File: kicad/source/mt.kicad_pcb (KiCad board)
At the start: 4 copper layers, 166.4 x 142.2 mm, 138 parts, among them IC1 MCP73831T-2ACI_OT, IC10 SN74HC148NSR, IC11 SN74HC148NSR, IC2 BQ29728DSER, IC3 TLV74333PDBVR, IC4 TLV9152IDR, IC5 MSPM0G3507SPMR, IC6 IS62WV1288BLL-55QLI, IC7 DAC082S085CIMMX_NOPB, IC8 SN74HC148NSR, IC9 SN74HC148NSR, J1 694106301002, J10 Conn_01x02_Pin, J2 3557-2, J3 SJ1-3524N, J4 Conn_01x05_Pin, J5 Conn_01x09_Pin, J6 Conn_01x03_Pin, J7 Conn_01x03_Pin, J8 Conn_01x03_Pin, J9 Conn_01x02_Pin, Q1 CSD16406Q3, Q2 CSD16406Q3, U1 1043

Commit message: misc adjustments
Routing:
- net GND: track 38.4 -> 42.3 mm, vias 14 -> 16
- net E2_2: track 83.4 -> 84.4 mm
- net Net-(IC11-6): track 59.2 -> 59.9 mm
- net E1_0: track 68.3 -> 67.8 mm

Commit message: completed PCB fab setup
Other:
- board text added: "5.5mm x 2.1mm 5V Only"
- board text removed: "6.5mm x 2.1mm 5V Only"
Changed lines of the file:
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@@
 			(outputformat 1)
 			(mirror no)
-			(drillshape 1)
+			(drillshape 0)
 			(scaleselection 1)
-			(outputdirectory "")
+			(outputdirectory "mt-fab/")
 		)
 	)
@@
 		(sheetname "/Rank 0/")
 		(sheetfile "rank.kicad_sch")
-		(attr smd)
+		(attr smd dnp)
 		(fp_line
 			(start -5.3 -2)
@@
 		(sheetname "/Rank 0/")
 		(sheetfile "rank.kicad_sch")
-		(attr smd)
+		(attr smd dnp)
 		(fp_line
 			(start -5.3 -2)
@@
 		(sheetname "/Rank 2/")
 		(sheetfile "rank.kicad_sch")
-		(attr smd)
+		(attr smd dnp)
 		(fp_line
 			(start -5.3 -2)
@@
 		(sheetname "/Rank 1/")
 		(sheetfile "rank.kicad_sch")
-		(attr smd)
+		(attr smd dnp)
 		(fp_line
 			(start -5.3 -2)
@@
 		(sheetname "/Rank 3/")
 		(sheetfile "rank.kicad_sch")
-		(attr smd)
+		(attr smd dnp)
 		(fp_line
 			(start -5.3 -2)
@@
 		(sheetname "/Rank 0/")
 		(sheetfile "rank.kicad_sch")
-		(attr smd)
+		(attr smd dnp)
 		(fp_line
 			(start -5.3 -2)
@@
 		(sheetname "/Rank 2/")
 		(sheetfile "rank.kicad_sch")
-		(attr smd)
+		(attr smd dnp)
 		(fp_line
 			(start -5.3 -2)
@@
 		(sheetname "/")
 		(sheetfile "mt.kicad_sch")
-		(attr smd)
+		(attr smd dnp)
 		(fp_line
 			(start -5.3 -2)
@@
 		(sheetname "/Rank 3/")
 		(sheetfile "rank.kicad_sch")
-		(attr smd)
+		(attr smd dnp)
 		(fp_line
 			(start -5.3 -2)
@@
 		(sheetname "/Rank 2/")
 		(sheetfile "rank.kicad_sch")
-		(attr smd)
+		(attr smd dnp)
 		(fp_line
 			(start -5.3 -2)
@@
 		(sheetname "/Rank 2/")
 		(sheetfile "rank.kicad_sch")
-		(attr smd)
+		(attr smd dnp)
 		(fp_line
 			(start -5.3 -2)
@@
 		(sheetname "/Rank 1/")
 		(sheetfile "rank.kicad_sch")
-		(attr smd)
+		(attr smd dnp)
 		(fp_line
 			(start -5.3 -2)
@@
 		(sheetname "/Rank 3/")
 		(sheetfile "rank.kicad_sch")
-		(attr smd)
+		(attr smd dnp)
 		(fp_line
 			(start -5.3 -2)
@@
 		(sheetname "/Rank 2/")
 		(sheetfile "rank.kicad_sch")
-		(attr smd)
+		(attr smd dnp)
 		(fp_line
 			(start -5.3 -2)
@@
 		(sheetname "/Rank 0/")
 		(sheetfile "rank.kicad_sch")
-		(attr smd)
+		(attr smd dnp)
 		(fp_line
 			(start -5.3 -2)
@@
 		(sheetname "/Rank 2/")
 		(sheetfile "rank.kicad_sch")
-		(attr smd)
+		(attr smd dnp)
 		(fp_line
 			(start -5.3 -2)
@@
 		(sheetname "/Rank 1/")
 		(sheetfile "rank.kicad_sch")
-		(attr smd)
+		(attr smd dnp)
 		(fp_line
 			(start -5.3 -2)
@@
 		(sheetname "/Rank 1/")
 		(sheetfile "rank.kicad_sch")
-		(attr smd)
+		(attr smd dnp)
 		(fp_line
 			(start -5.3 -2)
@@
 		(sheetname "/Rank 0/")
 		(sheetfile "rank.kicad_sch")
-		(attr smd)
+		(attr smd dnp)
 		(fp_line
 			(start -5.3 -2)
@@
 		(sheetname "/Rank 3/")
 		(sheetfile "rank.kicad_sch")
-		(attr smd)
+		(attr smd dnp)
 		(fp_line
 			(start -5.3 -2)
@@
 		(sheetname "/Rank 3/")
 		(sheetfile "rank.kicad_sch")
-		(attr smd)
+		(attr smd dnp)
 		(fp_line
 			(start -5.3 -2)
@@
 		(sheetname "/Rank 1/")
 		(sheetfile "rank.kicad_sch")
-		(attr smd)
+		(attr smd dnp)
 		(fp_line
 			(start -5.3 -2)
@@
 		(sheetname "/Rank 2/")
 		(sheetfile "rank.kicad_sch")
-		(attr smd)
+		(attr smd dnp)
 		(fp_line
 			(start -5.3 -2)
@@
 		(sheetname "/Rank 1/")
 		(sheetfile "rank.kicad_sch")
-		(attr smd)
+		(attr smd dnp)
 		(fp_line
 			(start -5.3 -2)
@@
 		(sheetname "/Rank 0/")
 		(sheetfile "rank.kicad_sch")
-		(attr smd)
+		(attr smd dnp)
 		(fp_line
 			(start -5.3 -2)
@@
 		(sheetname "/Rank 3/")
 		(sheetfile "rank.kicad_sch")
-		(attr smd)
+		(attr smd dnp)
 		(fp_line
 			(start -5.3 -2)
@@
 		(sheetname "/Rank 1/")
 		(sheetfile "rank.kicad_sch")
-		(attr smd)
+		(attr smd dnp)
 		(fp_line
 			(start -5.3 -2)
@@
 		(sheetname "/Rank 3/")
 		(sheetfile "rank.kicad_sch")
-		(attr smd)
+		(attr smd dnp)
 		(fp_line
 			(start -5.3 -2)
@@
 		(sheetname "/")
 		(sheetfile "mt.kicad_sch")
-		(attr smd)
+		(attr smd dnp)
 		(fp_line
 			(start -5.3 -2)
@@
 		(sheetname "/Rank 0/")
 		(sheetfile "rank.kicad_sch")
-		(attr smd)
+		(attr smd dnp)
 		(fp_line
 			(start -5.3 -2)
@@
 		(sheetname "/Rank 2/")
 		(sheetfile "rank.kicad_sch")
-		(attr smd)
+		(attr smd dnp)
 		(fp_line
 			(start -5.3 -2)
@@
 		(sheetname "/Rank 3/")
 		(sheetfile "rank.kicad_sch")
-		(attr smd)
+		(attr smd dnp)
 		(fp_line
 			(start -5.3 -2)
@@
 		(sheetname "/Rank 0/")
 		(sheetfile "rank.kicad_sch")
-		(attr smd)
+		(attr smd dnp)
 		(fp_line
 			(start -5.3 -2)
@@
 		(sheetname "/Rank 1/")
 		(sheetfile "rank.kicad_sch")
-		(attr smd)
+		(attr smd dnp)
 		(fp_line
 			(start -5.3 -2)
@@
 		)
 	)
-	(gr_text "6.5mm x\n2.1mm\n5V Only"
+	(gr_text "5.5mm x\n2.1mm\n5V Only"
 		(at 56.515 38.735 0)
 		(layer "F.SilkS")

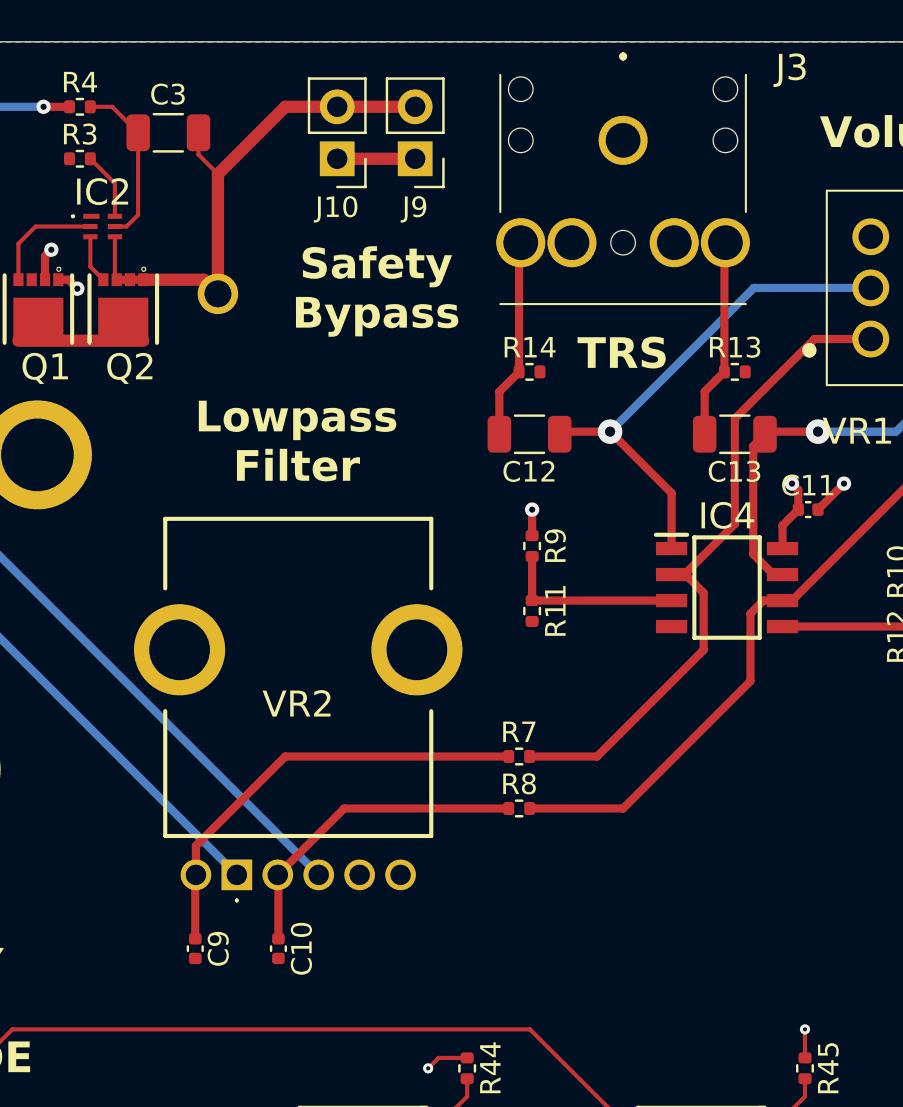
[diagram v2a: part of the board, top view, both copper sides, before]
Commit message: adjusted PCB fab setup for faster manufacturing
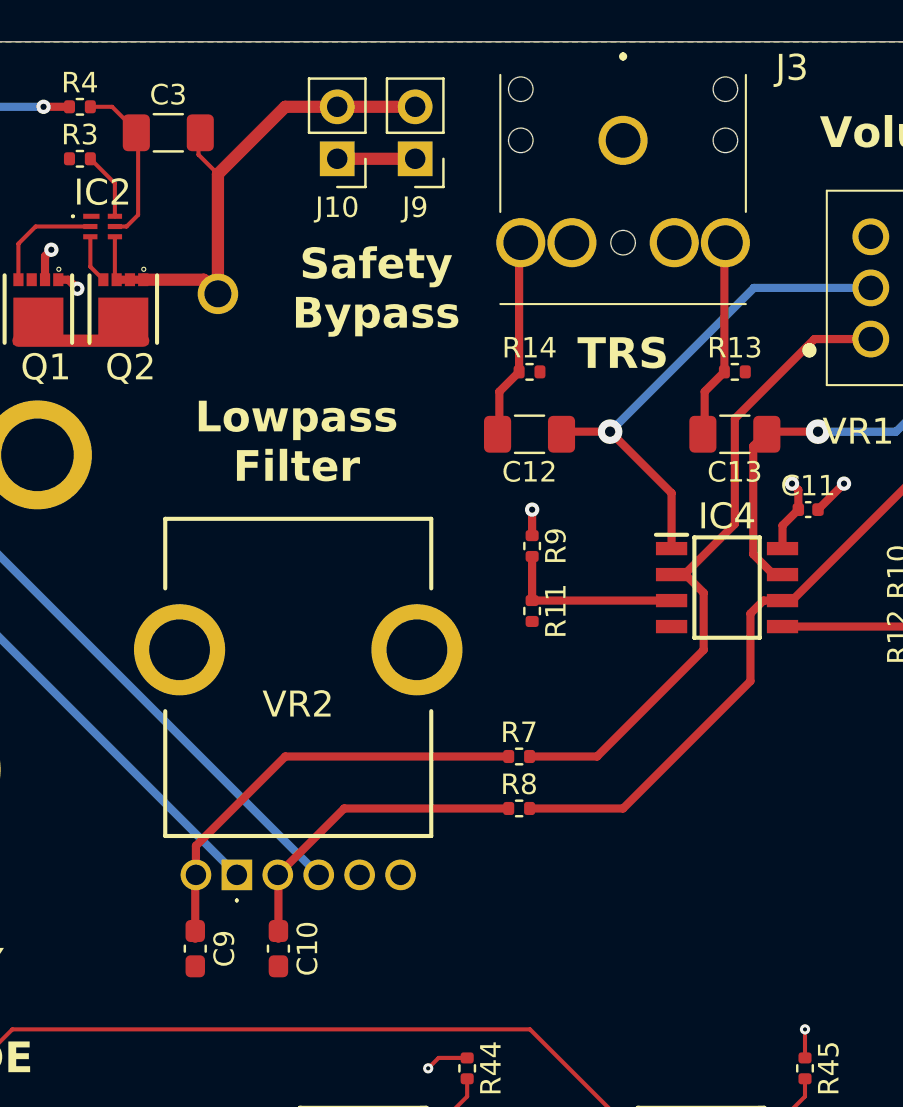
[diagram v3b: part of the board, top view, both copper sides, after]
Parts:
- C10, C9: footprint Capacitor_SMD:C_0402_1005Metric -> Capacitor_SMD:C_0603_1608Metric_Pad1.08x0.95mm_HandSolder
- C12, C13, C3: footprint Capacitor_SMD:C_1206_3216Metric -> Capacitor_SMD:C_1206_3216Metric_Pad1.33x1.80mm_HandSolder
